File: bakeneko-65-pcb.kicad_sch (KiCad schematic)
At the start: 23 parts, among them J1 JST SH 4-pin, J2 AVR-ISP-6, J3 Conn_01x06_Female, SW1 Reset, U1 SRV05-4, U2 ATmega32U4-AU, Y1 16MHz

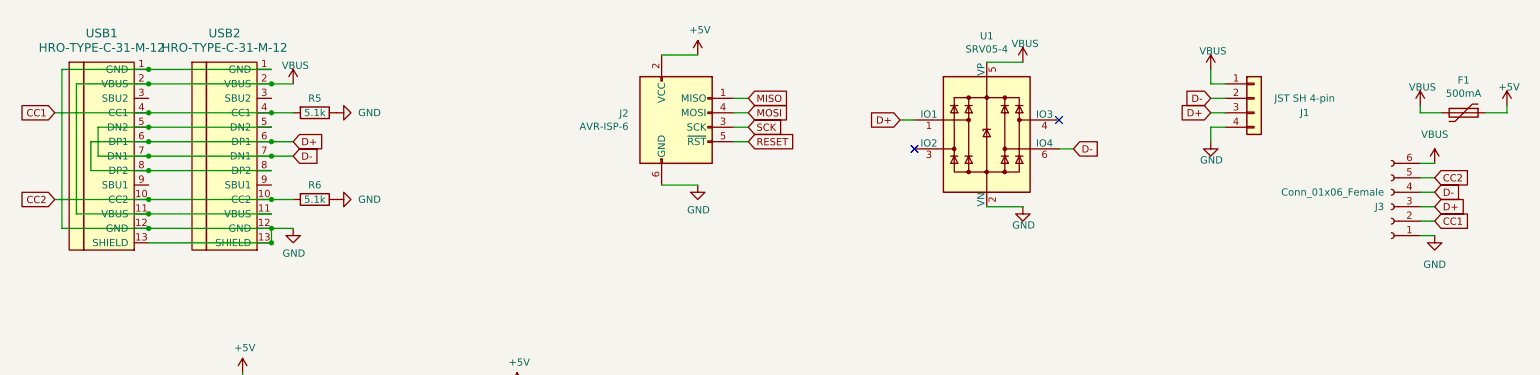
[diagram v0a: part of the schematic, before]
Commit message: remove usb
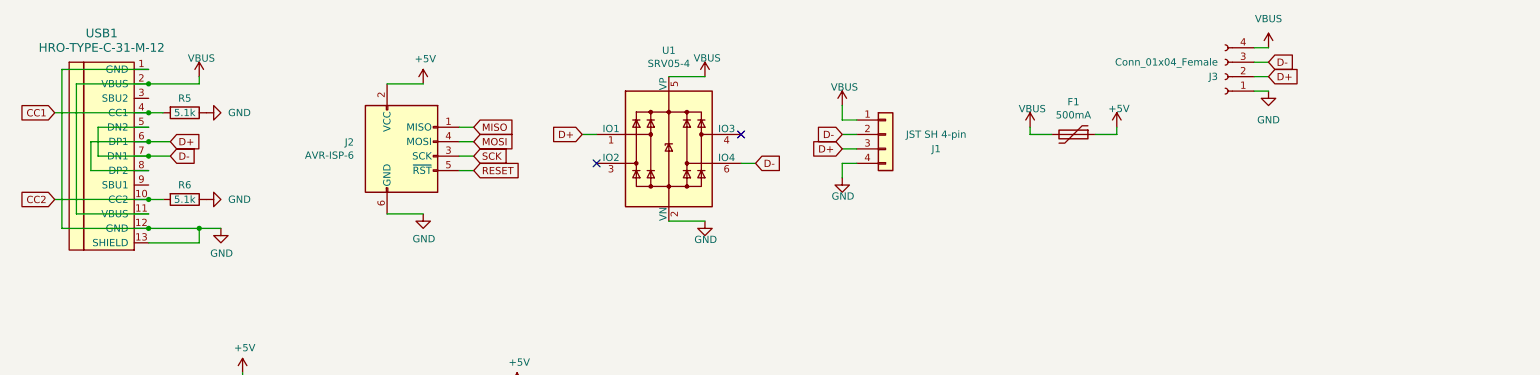
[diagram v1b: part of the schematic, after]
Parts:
- removed J3: Conn_01x06_Female, Connector_PinHeader_1.00mm:PinHeader_1x06_P1.00mm_Vertical, symbol Connector:Conn_01x06_Female
- removed USB2: HRO-TYPE-C-31-M-12, Type-C:HRO-TYPE-C-31-M-12, symbol Type-C:HRO-TYPE-C-31-M-12
- added J3: Conn_01x04_Female, Connector_PinHeader_1.00mm:PinHeader_1x04_P1.00mm_Vertical, symbol Connector:Conn_01x04_Female
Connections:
- net D+: now also J3.2 (Pin_2)
- net D-: now also J3.3 (Pin_3)
- net GND: now also J3.1 (Pin_1)
- net VBUS: now also J3.4 (Pin_4)
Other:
- moved on the sheet: F1, J1, J2, R5, R6, U1

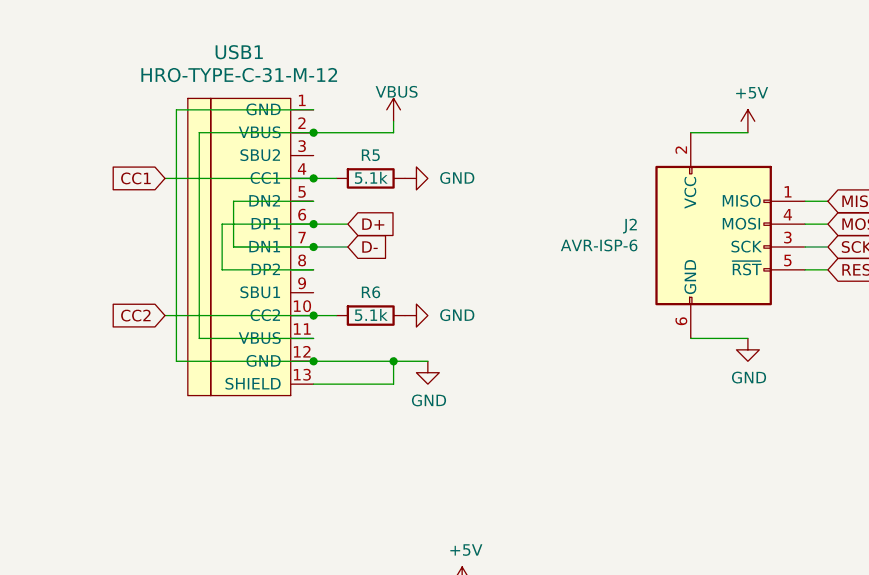
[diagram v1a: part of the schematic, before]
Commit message: add USB c
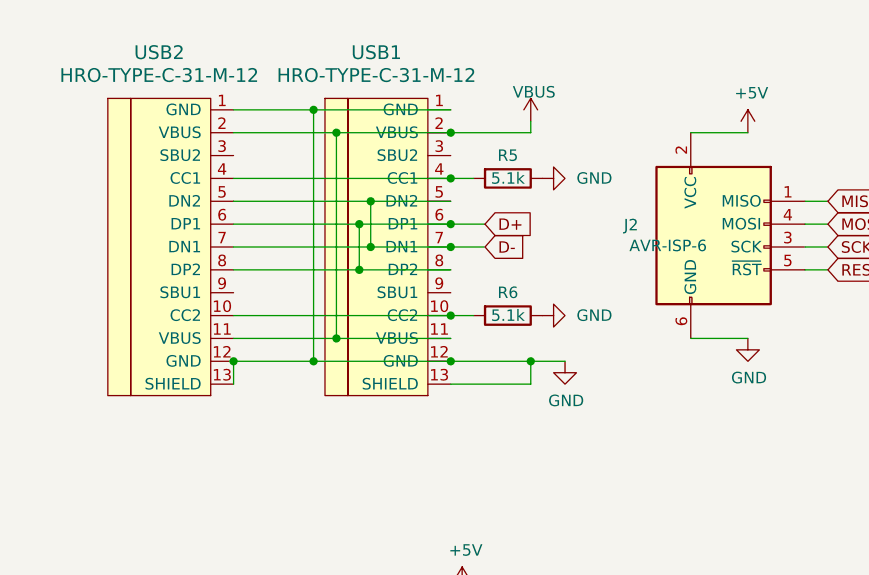
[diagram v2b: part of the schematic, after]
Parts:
- added USB2: HRO-TYPE-C-31-M-12, Type-C:HRO-TYPE-C-31-M-12, symbol Type-C:HRO-TYPE-C-31-M-12
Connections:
- net D+: now also USB2.6 (DP1), USB2.8 (DP2)
- net D-: now also USB2.5 (DN2), USB2.7 (DN1)
- net GND: now also USB2.1 (GND), USB2.12 (GND), USB2.13 (SHIELD)
- net VBUS: now also USB2.11 (VBUS), USB2.2 (VBUS)
- net CC1: no longer names the net of R5.2, USB1.4 (CC1)
- net CC1: now also USB2.4 (CC1)
- net CC2: no longer names the net of R6.2, USB1.10 (CC2)
- net CC2: now also USB2.10 (CC2)
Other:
- moved on the sheet: R5, R6, USB1

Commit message: change Atmega AU to MU
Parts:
- U2: footprint Package_QFP:TQFP-44_10x10mm_P0.8mm -> tahutech:Hybrid Atmega32u4
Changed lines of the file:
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@@
       (effects (font (size 1.27 1.27)))
     )
-    (property "Footprint" "Package_QFP:TQFP-44_10x10mm_P0.8mm" (at 58.42 128.27 0)
+    (property "Footprint" "tahutech:Hybrid Atmega32u4" (at 58.42 128.27 0)
       (effects (font (size 1.27 1.27) italic) hide)
     )
